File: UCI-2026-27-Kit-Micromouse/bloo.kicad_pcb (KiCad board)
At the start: 2 copper layers, 100 x 100 mm, 93 parts, among them J5 SWD_Header, M1 M1_Conn_Alt, M2 M2_Conn_Alt, Q0 TEFT4300, Q1 TEFT4300, Q10 Q_NMOS_GSD, Q11 Q_NMOS_GSD, Q12 Q_NMOS_GSD, Q2 TEFT4300, Q3 TEFT4300, Q9 Q_NMOS_GSD, U1 YAAJ_BluePill_SWD_Breakout, U2 L293D, U3 LM1085-5.0, U4 NCP161ASN330T1G, U5 BC832, Y1 ABS07-32.768KHZ-T

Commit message: added power supply section. couldn't place L1, but will find it later.
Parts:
- moved JP4 155.4 mm to (48.6, 108.5)
- moved R17 143.9 mm to (47.0, 38.5)
- moved C13 109.3 mm to (85.1, 31.5)
- moved U4 105.2 mm to (102.1, 31.4)
- moved R23 100.4 mm to (96.5, 31.5)
- moved C1 97.4 mm to (90.5, 31.5)
- moved C17 91.4 mm to (108.1, 31.5)
- moved M1 91.1 mm to (58.0, 55.5)
- moved BT1 90.9 mm to (103.0, 40.5)
- moved C10 90.8 mm to (106.9, 24.0)
- moved TP2 88.5 mm to (54.5, 109.0)
- moved C18 84.8 mm to (114.6, 36.5)
- moved C9 84.3 mm to (112.4, 24.0)
- moved C15 84.2 mm to (114.4, 31.5)
- moved R22 80.0 mm to (118.0, 24.0)
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
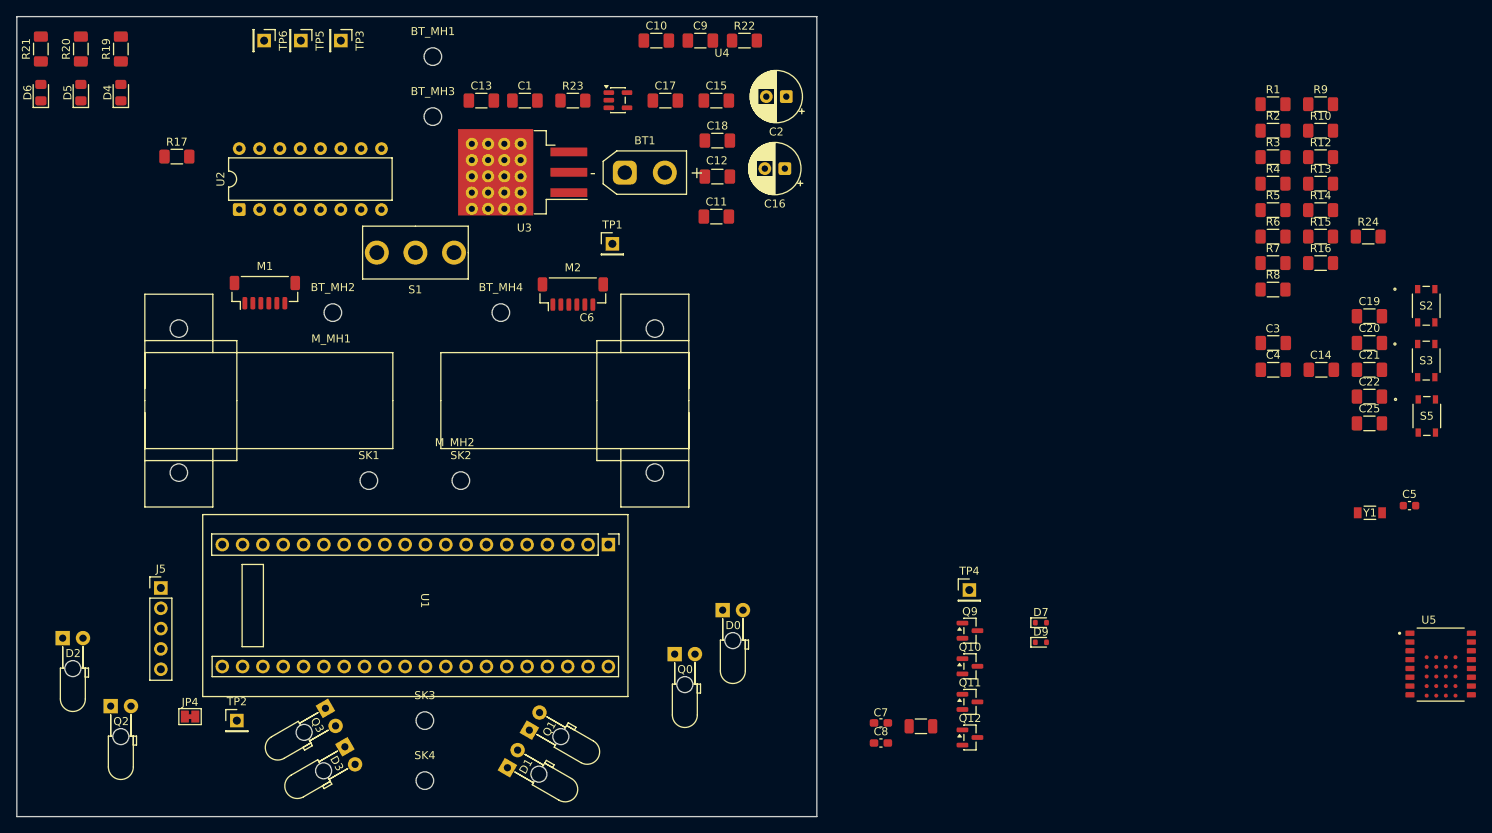
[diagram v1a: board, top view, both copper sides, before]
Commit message: about to change power supply layout to make more room for sensors
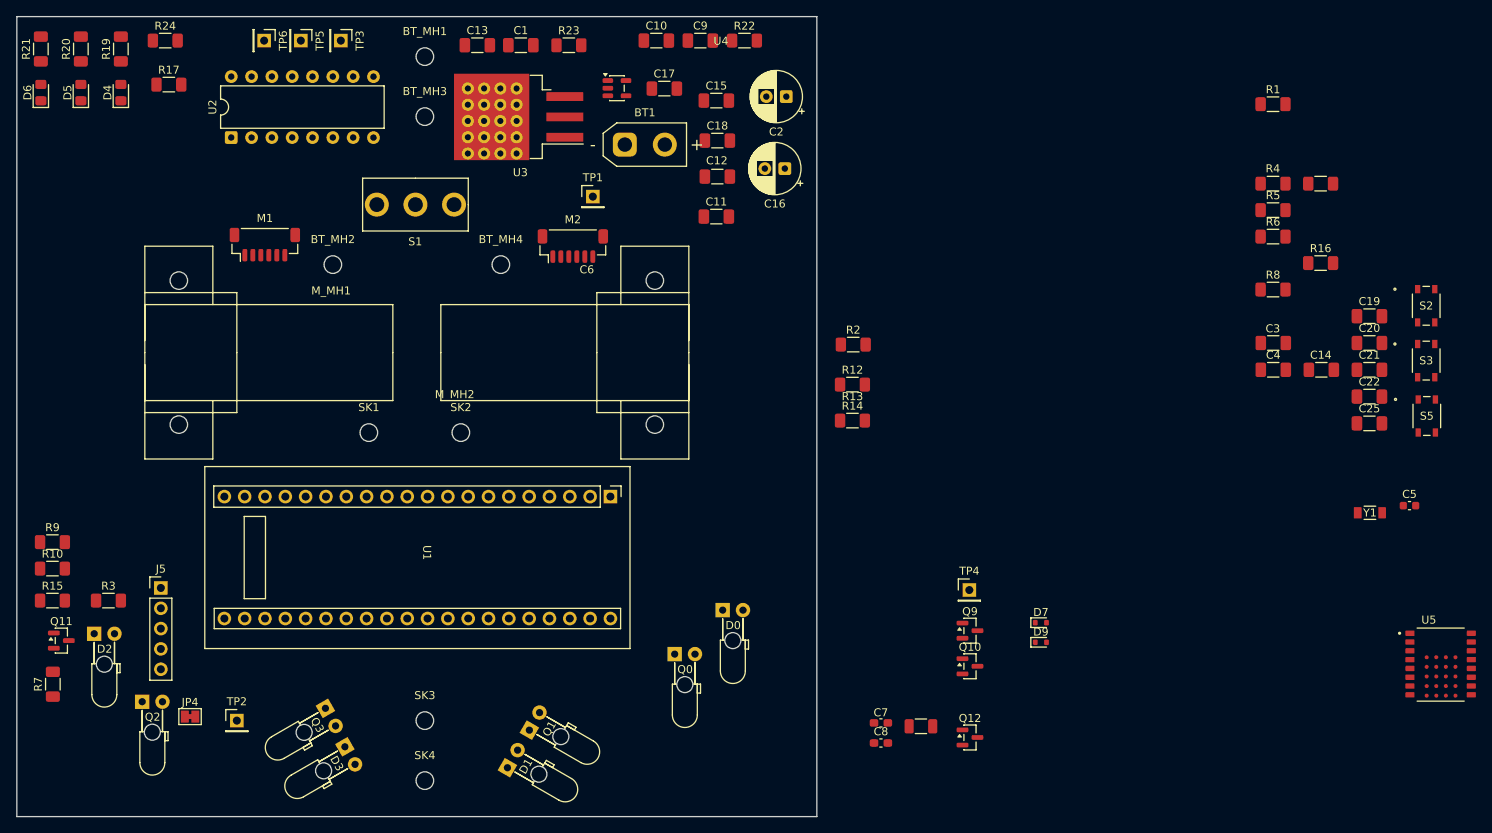
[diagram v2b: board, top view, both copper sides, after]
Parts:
- moved R10 167.7 mm to (31.4, 90.0)
- moved R9 167.7 mm to (31.4, 86.7)
- moved R15 164.9 mm to (31.4, 94.0)
- moved R7 161.4 mm to (31.5, 104.5), turned to 90 degrees
- moved R3 155.8 mm to (38.5, 94.0)
- moved R24 152.4 mm to (45.5, 24.0)
- moved Q11 113.8 mm to (32.6, 99.0)
- moved R12 65.1 mm to (131.4, 67.0)
- moved R14 64.2 mm to (131.4, 71.5)
- moved R2 58.9 mm to (131.6, 62.0)
- moved R17 9.06 mm to (46.0, 29.5)
- moved U2 9.06 mm to (53.8, 36.1)
- moved C1 6.94 mm to (90.0, 24.6)
- moved C13 6.94 mm to (84.6, 24.6)
- moved R23 6.94 mm to (96.0, 24.6)
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
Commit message: added sensor section. will need to move stuff around in this section to make room for V5.
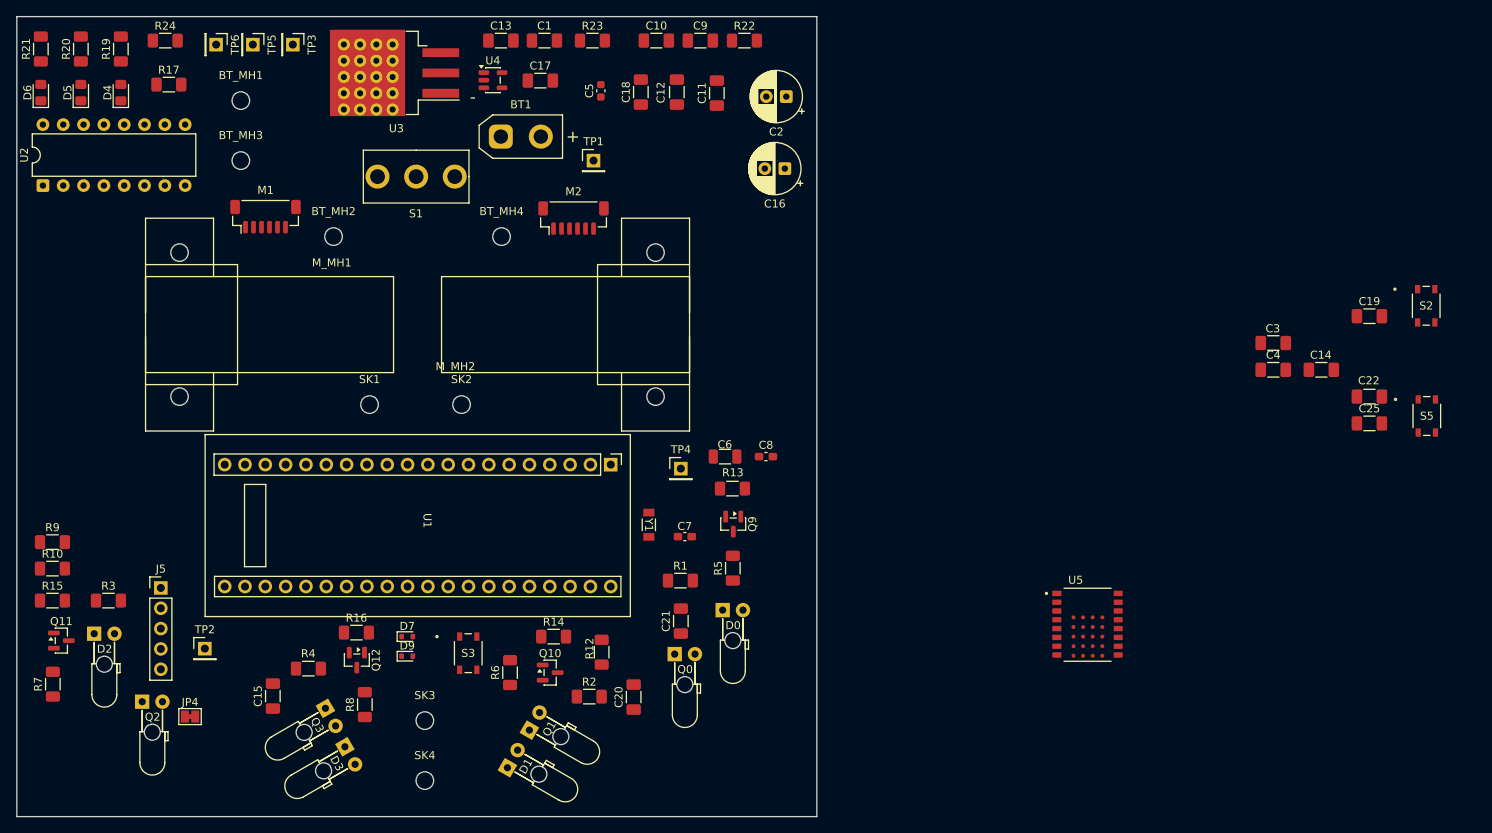
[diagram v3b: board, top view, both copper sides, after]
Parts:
- moved R4 135.0 mm to (63.5, 102.5)
- moved R16 129.1 mm to (69.5, 98.0)
- moved S3 125.2 mm to (83.4, 100.6)
- moved R8 124.8 mm to (70.5, 107.0), turned to 90 degrees
- moved C5 113.6 mm to (100.0, 30.3), turned to 90 degrees
- moved R6 109.8 mm to (88.7, 103.0), turned to 90 degrees
- moved C20 102.1 mm to (104.1, 106.1), turned to 90 degrees
- moved R1 95.0 mm to (110.0, 91.5)
- moved C15 92.8 mm to (59.0, 105.9), turned to 90 degrees
- moved C21 91.6 mm to (110.0, 96.6), turned to 90 degrees
- moved Y1 90.1 mm to (106.0, 84.5), turned to -90 degrees
- moved R13 82.8 mm to (116.5, 80.0)
- moved R5 81.0 mm to (116.5, 90.0), turned to 90 degrees
- moved D7 79.2 mm to (75.8, 98.5)
- moved D9 79.2 mm to (75.8, 101.0)
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
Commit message: finished placing down components. will need to make changes to account for rat nest lines.
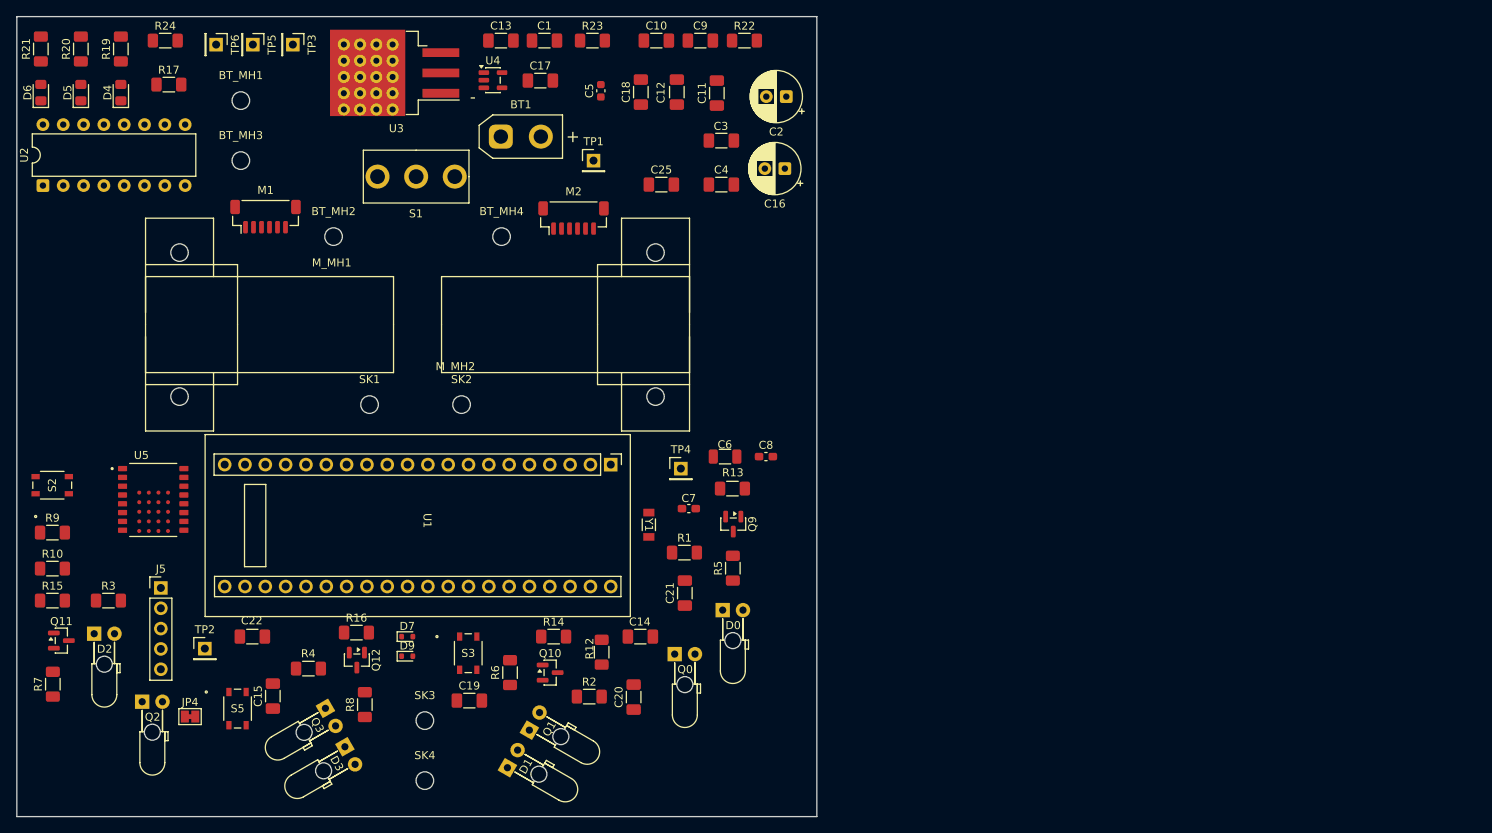
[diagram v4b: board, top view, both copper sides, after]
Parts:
- moved S2 173.2 mm to (31.4, 79.6), turned to 90 degrees
- moved S5 153.1 mm to (54.6, 107.5)
- moved C22 142.8 mm to (56.4, 98.5)
- moved C19 122.3 mm to (83.6, 106.5)
- moved U5 117.8 mm to (44.0, 81.4)
- moved C25 93.4 mm to (107.6, 42.0)
- moved C14 91.4 mm to (104.9, 98.5)
- moved C3 73.5 mm to (115.1, 36.5)
- moved C4 72.8 mm to (115.1, 42.0)
- moved C21 3.54 mm to (110.5, 93.1)
- moved C7 3.54 mm to (111.0, 82.5)
- moved R1 3.54 mm to (110.5, 88.0)
- moved R9 1.19 mm to (31.4, 85.5)
